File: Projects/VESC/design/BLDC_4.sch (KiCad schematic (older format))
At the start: 26 parts, among them K1 SERVO, P1 HALL/Encoder, P101 CANBUS, P3 PWR_COMM, P4 IN+, P5 IN-, P6 MOTOR1, P7 MOTOR2, P9 MOTOR3, X1 MINI-USB-SHIELD-32005-201

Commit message: More schematic updates for VESC
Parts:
- removed C3: 100n, Capacitors_SMD:C_0805, symbol C-RESCUE-BLDC_4
- removed K1: SERVO, CRF1:pinhead-1X03, symbol CONN_3
- removed P1: HALL/Encoder, CRF1:MICRO_JST_6, symbol CONN_6
- removed P101: CANBUS, JST conn:b4b-ph-kl, symbol CONN_4
- removed P3: PWR_COMM, CRF1:b7b-ph-kl, symbol CONN_01X07
- removed P4: IN+, CRF1:1PAD_4x5mm, symbol CONN_1
- removed P5: IN-, CRF1:1PAD_4x5mm, symbol CONN_1
- removed P6: MOTOR1, CRF1:1PAD_4x5mm, symbol CONN_1
- removed P7: MOTOR2, CRF1:1PAD_4x5mm, symbol CONN_1
- removed P9: MOTOR3, CRF1:1PAD_4x5mm, symbol CONN_1
- removed R5: 2k2, Resistors_SMD:R_0805, symbol R-RESCUE-BLDC_4
- removed R6: 0R, Resistors_SMD:R_0805, symbol R-RESCUE-BLDC_4
- removed X1: MINI-USB-SHIELD-32005-201, CRF1:USB-UX60R-MB-5ST, symbol MINI-USB-SCHIELD-32005-201
- added JP1, JP2, JP3: Jumper_NC_Small, USST-footprints:J_0805, symbol Jumper_NC_Small
- added JP4, JP7, JP8, JP9: Jumper_NC_Small, USST-footprints:J_0805, symbol Jumper_NO_Small
- C2: symbol C-RESCUE-BLDC_4 -> C
- D1, D2, D3: symbol LED-RESCUE-BLDC_4 -> LED
- R103, R104, R22, R3, R37, R38, R4: symbol R-RESCUE-BLDC_4 -> R
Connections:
- net Filters/HALL1_OUT: now also JP3.1
- net Filters/HALL2_OUT: now also JP2.1
- net Filters/HALL3_OUT: now also JP1.1
- net GND: now also D1.1 (K), D2.1 (K), D3.1 (K); no longer D1.2 (K), D2.2 (K), D3.2 (K)
- net RX_SCL_MOSI: now also JP9.1
- net TX_SDA: now also JP4.2
- net VCC: now also JP9.2
- net USB_DM: now reaches R103.2
- net USB_DP: now reaches R104.2
- net at R38.1: now also D2.2 (A); no longer D2.1 (A)
- net at R37.1: now also D1.2 (A); no longer D1.1 (A)
- net at R22.1: now also D3.2 (A); no longer D3.1 (A)
- new net CS: JP3.2, JP4.1
- new net MISO: JP2.2, JP7.1
- new net MISO_2: JP7.2
- new net SCK: JP1.2, JP8.1
- new net SCK_2: JP8.2
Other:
- note added: "Servo Output Unused"
- note removed: "100R if used as\nservo output"
- note removed: "Mount 0R if used\nas USB host"
- moved on the sheet: C2, D1, D2, D3, R103, R104, R22, R3, R37, R38, R4, R53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

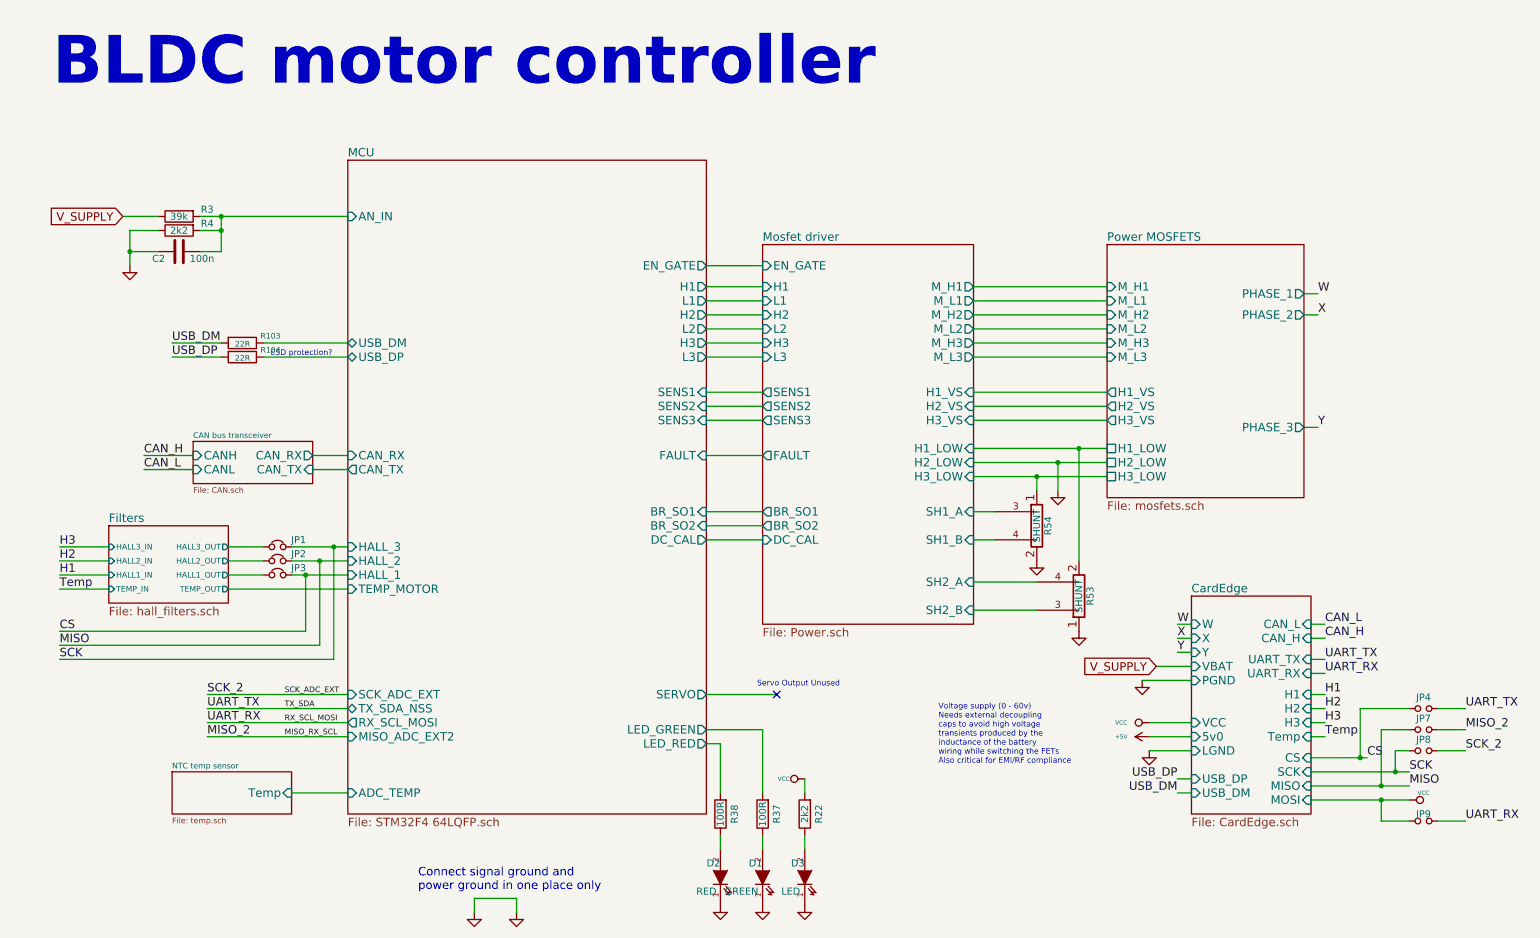
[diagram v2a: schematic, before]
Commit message: completing VESC card layout
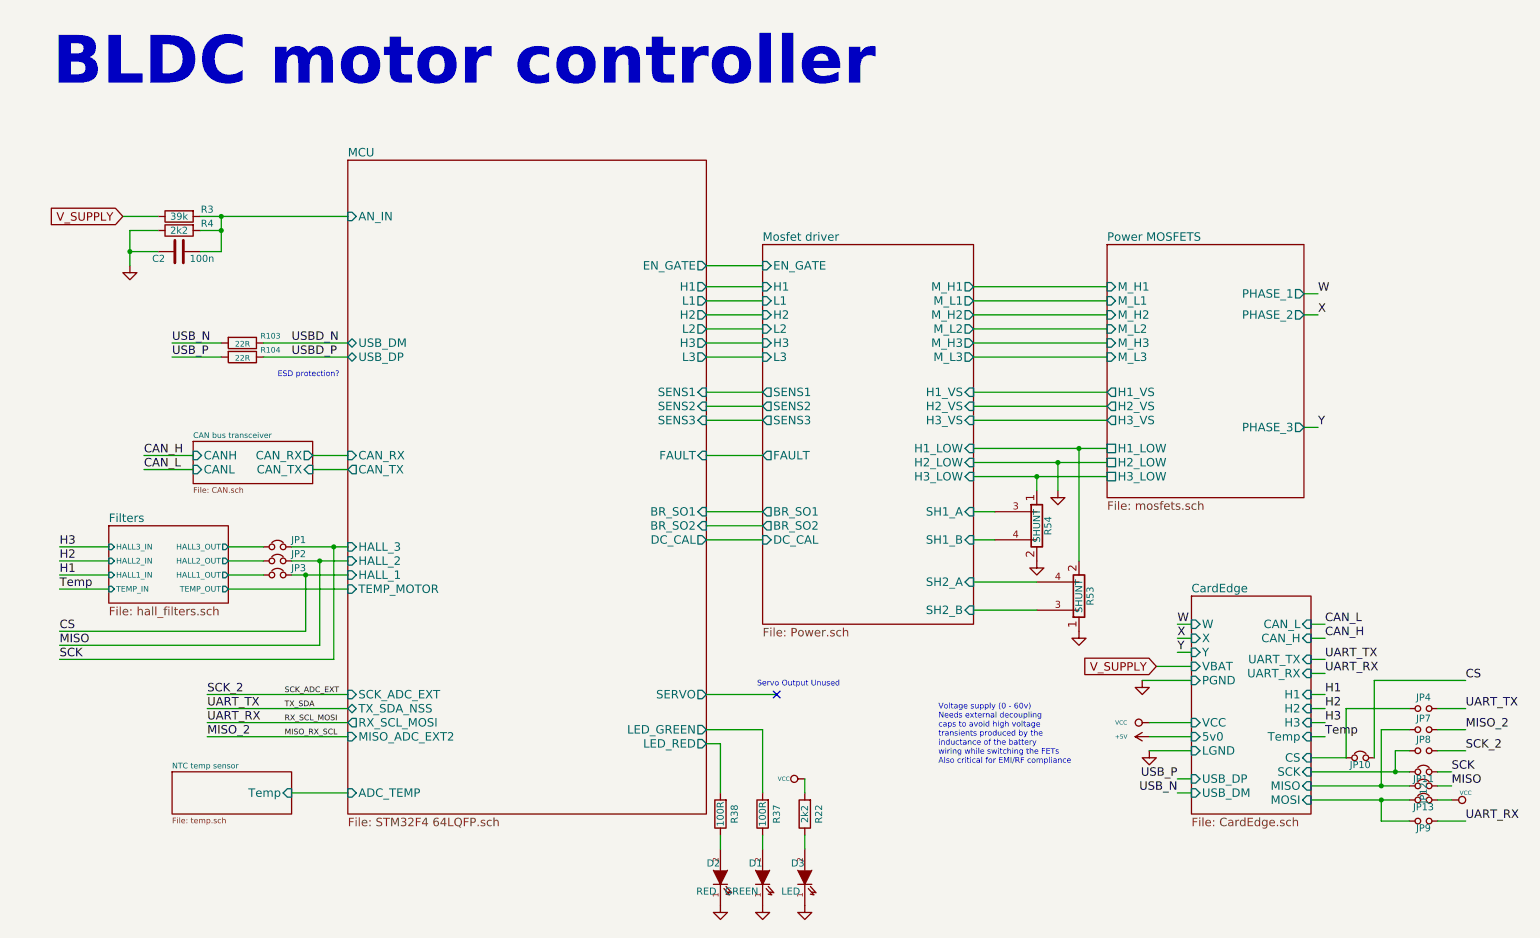
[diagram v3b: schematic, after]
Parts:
- added JP10, JP11, JP12, JP13: Jumper_NC_Small, USST-footprints:J_0603, symbol Jumper_NC_Small
- JP1, JP2, JP3, JP4, JP7, JP8, JP9: footprint USST-footprints:J_0805 -> USST-footprints:J_0603
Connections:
- net CS: now also JP10.2; no longer JP4.1
- net GND: no longer D1.1 (K), D2.1 (K), D3.1 (K)
- net MISO: now also JP12.2; no longer JP7.1
- net RX_SCL_MOSI: now also JP9.2; no longer JP9.1
- net SCK: now also JP11.2; no longer JP8.1
- net VCC: now also JP13.2; no longer JP9.2
- net MCU/USB_DM renamed USBD_N
- net MCU/USB_DP renamed USBD_P
- net USB_DM renamed USB_N
- net USB_DP renamed USB_P
- new net CardEdge/CS: JP10.1, JP4.1
- new net CardEdge/MISO: JP12.1, JP7.1
- new net CardEdge/MOSI: JP13.1, JP9.1
- new net CardEdge/SCK: JP11.1, JP8.1
- new net GNDD: D1.1 (K), D2.1 (K), D3.1 (K)
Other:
- note removed: "Connect signal ground and\npower ground in one place only"
